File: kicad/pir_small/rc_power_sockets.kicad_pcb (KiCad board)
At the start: 2 copper layers, 25.4 x 25.4 mm, 26 parts, among them IC1 ATTINY85, J1 GND, J2 433MHZ, P1 ICSP, P2 ALT_PWR, Q1 NMOS, Q2 PMOS, U1 MCP1755ST-3302E/DB

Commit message: Changed layout
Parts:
- removed ON   OFF: SWITCH_INV, Buttons_Switches_ThroughHole:SW_Micro_SPST
- removed RV1: POT, Pin_Headers:Pin_Header_Straight_1x03
- added P3: CONN_01X01, theapi_footprints:SMD_PAD, F.Cu at (149.2, 70.4)
- added P4: CONN_01X01, theapi_footprints:SMD_PAD, F.Cu at (149.2, 67.9)
- added SW1: SWITCH_INV, Buttons_Switches_ThroughHole:SW_Micro_SPST, F.Cu at (164.4, 87.0)
- D1, D2, D3: footprint theapi_footprints:SOD-123-Schottky -> theapi_footprints:SOD-123-handsolder
- IC1: footprint theapi_footprints:SOIC-8-N-hand-sold -> theapi_footprints:SOIC-8-N-handsolder
- J1: value GND -> PIR; moved to B.Cu
- P2: footprint Pin_Headers:Pin_Header_Straight_1x02 -> Socket_Strips:Socket_Strip_Straight_1x02
- R5: value 820R -> 820
- moved D4 61.6 mm to (149.2, 82.7), turned to 270 degrees
- moved R5 58.7 mm to (151.6, 82.6), turned to 270 degrees
- moved Q2 54.3 mm to (154.0, 80.1), turned to 90 degrees
- moved D1 51.9 mm to (157.3, 81.2), turned to 0 degrees
- moved D2 51.7 mm to (157.3, 79.1), turned to 0 degrees
- moved C2 48.0 mm to (156.8, 77.6), turned to 180 degrees
- moved R2 47.5 mm to (161.2, 82.0), turned to 180 degrees
- moved U1 46.9 mm to (162.4, 74.8)
- moved Q1 44.7 mm to (154.0, 83.9)
- moved R3 44.5 mm to (149.7, 82.9)
- moved J1 44.0 mm to (170.8, 73.6)
- moved MOUNT6 43.6 mm to (170.8, 65.4)
- moved MOUNT2 43.6 mm to (170.8, 87.0)
- moved J2 43.4 mm to (149.2, 78.7)
- moved IC1 43.4 mm to (157.0, 75.0)
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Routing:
- net /NBASE_ON: track 25.7 -> 8.84 mm
- net /ADC3: track 22.7 -> 7.33 mm
- net /PBASE: track 22.8 -> 9.69 mm
- net /RESET: track 12.1 -> 20.9 mm, vias 1 -> 2
- net /NBASE: track 5.39 -> 14.0 mm
- net /SWITCH_POWER: track 49.2 -> 42.8 mm, vias 3 -> 0
- net /VCC: track 5.59 -> 2.79 mm
- net /MISO: track 21.3 -> 23.8 mm
- net GND: track 121.1 -> 123.2 mm, vias 4 -> 3
- net /3.3v: track 32.3 -> 30.5 mm
- net /SCK: track 33.4 -> 31.7 mm, vias 0 -> 1
- net /MOSI: track 34.8 -> 33.4 mm
- net /POWER: track 22.8 -> 22.0 mm
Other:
- board size 25.4 x 25.4 mm -> 25 x 25 mm

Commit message: Silkscreen
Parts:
- P3, P4: footprint theapi_footprints:SMD_PAD -> Pin_Headers:Pin_Header_Straight_1x01
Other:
- board text added: "+"
- board text added: "-"
- board text added: "1"
- board text added: "A0"
- board text added: "D"
- board text added: "ON OFF"
- board text added: "PIR"
- board text added: "RC Power Sockets Small v1.0"
- board text removed: "GND"
- board text removed: "RC Power Sockets v2.0"
- board text removed: "SCK"
- board text removed: "VCC"

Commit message: Power pins
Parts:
- P2: footprint Socket_Strips:Socket_Strip_Straight_1x02 -> Pin_Headers:Pin_Header_Straight_1x02
- turned P2 to 90 degrees
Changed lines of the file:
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@@
     (links 49)
     (no_connects 0)
-    (area 147.382999 63.582999 172.533001 88.733001)
+    (area 144.000667 61.624 175.915334 93.082)
     (thickness 1.6)
-    (drawings 35)
+    (drawings 33)
     (tracks 197)
     (zones 0)
@@
   (page A4)
   (layers
-    (0 F.Cu signal hide)
-    (31 B.Cu signal hide)
+    (0 F.Cu signal)
+    (31 B.Cu signal)
     (32 B.Adhes user)
     (33 F.Adhes user)
@@
     (35 F.Paste user)
     (36 B.SilkS user)
-    (37 F.SilkS user hide)
+    (37 F.SilkS user)
     (38 B.Mask user)
     (39 F.Mask user)
@@
     )
   )
-  (module Socket_Strips:Socket_Strip_Straight_1x02 (layer F.Cu)
-    (at 156.529 86.953)
-    (descr "Through hole socket strip")
-    (tags "socket strip")
-    (fp_text reference P2 (at 0 -5.1) (layer F.SilkS) hide
-      (effects (font (size 1 1) (thickness 0.15)))
-    )
-    (fp_text value ALT_PWR (at 0 -3.1) (layer F.Fab) hide
-      (effects (font (size 1 1) (thickness 0.15)))
-    )
-    (fp_line (start -1.55 1.55) (end 0 1.55) (layer F.SilkS) (width 0.15))
-    (fp_line (start 3.81 1.27) (end 1.27 1.27) (layer F.SilkS) (width 0.15))
-    (fp_line (start -1.75 -1.75) (end -1.75 1.75) (layer F.CrtYd) (width 0.05))
-    (fp_line (start 4.3 -1.75) (end 4.3 1.75) (layer F.CrtYd) (width 0.05))
-    (fp_line (start -1.75 -1.75) (end 4.3 -1.75) (layer F.CrtYd) (width 0.05))
-    (fp_line (start -1.75 1.75) (end 4.3 1.75) (layer F.CrtYd) (width 0.05))
-    (fp_line (start 1.27 1.27) (end 1.27 -1.27) (layer F.SilkS) (width 0.15))
-    (fp_line (start 0 -1.55) (end -1.55 -1.55) (layer F.SilkS) (width 0.15))
-    (fp_line (start -1.55 -1.55) (end -1.55 1.55) (layer F.SilkS) (width 0.15))
-    (fp_line (start 1.27 -1.27) (end 3.81 -1.27) (layer F.SilkS) (width 0.15))
-    (fp_line (start 3.81 -1.27) (end 3.81 1.27) (layer F.SilkS) (width 0.15))
-    (pad 1 thru_hole rect (at 0 0) (size 2.032 2.032) (drill 1.016) (layers *.Cu *.Mask F.SilkS)
-      (net 1 GND))
-    (pad 2 thru_hole oval (at 2.54 0) (size 2.032 2.032) (drill 1.016) (layers *.Cu *.Mask F.SilkS)
-      (net 16 /VCC))
-    (model Socket_Strips.3dshapes/Socket_Strip_Straight_1x02.wrl
-      (at (xyz 0.05 0 0))
-      (scale (xyz 1 1 1))
-      (rotate (xyz 0 0 180))
-    )
-  )
   (module Pin_Headers:Pin_Header_Straight_1x01 (layer F.Cu)
     (at 149.163 70.443)
@@
     )
   )
+  (module Pin_Headers:Pin_Header_Straight_1x02 (layer F.Cu)
+    (at 156.529 86.953 90)
+    (descr "Through hole pin header")
+    (tags "pin header")
+    (fp_text reference P2 (at 0 -5.1 90) (layer F.SilkS) hide
+      (effects (font (size 1 1) (thickness 0.15)))
+    )
+    (fp_text value ALT_PWR (at 0 -3.1 90) (layer F.Fab) hide
+      (effects (font (size 1 1) (thickness 0.15)))
+    )
+    (fp_line (start 1.27 1.27) (end 1.27 3.81) (layer F.SilkS) (width 0.15))
+    (fp_line (start 1.55 -1.55) (end 1.55 0) (layer F.SilkS) (width 0.15))
+    (fp_line (start -1.75 -1.75) (end -1.75 4.3) (layer F.CrtYd) (width 0.05))
+    (fp_line (start 1.75 -1.75) (end 1.75 4.3) (layer F.CrtYd) (width 0.05))
+    (fp_line (start -1.75 -1.75) (end 1.75 -1.75) (layer F.CrtYd) (width 0.05))
+    (fp_line (start -1.75 4.3) (end 1.75 4.3) (layer F.CrtYd) (width 0.05))
+    (fp_line (start 1.27 1.27) (end -1.27 1.27) (layer F.SilkS) (width 0.15))
+    (fp_line (start -1.55 0) (end -1.55 -1.55) (layer F.SilkS) (width 0.15))
+    (fp_line (start -1.55 -1.55) (end 1.55 -1.55) (layer F.SilkS) (width 0.15))
+    (fp_line (start -1.27 1.27) (end -1.27 3.81) (layer F.SilkS) (width 0.15))
+    (fp_line (start -1.27 3.81) (end 1.27 3.81) (layer F.SilkS) (width 0.15))
+    (pad 1 thru_hole rect (at 0 0 90) (size 2.032 2.032) (drill 1.016) (layers *.Cu *.Mask F.SilkS)
+      (net 1 GND))
+    (pad 2 thru_hole oval (at 0 2.54 90) (size 2.032 2.032) (drill 1.016) (layers *.Cu *.Mask F.SilkS)
+      (net 16 /VCC))
+    (model Pin_Headers.3dshapes/Pin_Header_Straight_1x02.wrl
+      (at (xyz 0 -0.05 0))
+      (scale (xyz 1 1 1))
+      (rotate (xyz 0 0 90))
+    )
+  )
   (gr_text A0 (at 151.449 70.316) (layer B.SilkS)
     (effects (font (size 1.016 1.016) (thickness 0.1524)) (justify mirror))
@@
     (effects (font (size 1.016 1.016) (thickness 0.1524)))
   )
-  (gr_line (start 142.458 76.158) (end 174.958 76.158) (angle 90) (layer Cmts.User) (width 0.2))
-  (gr_line (start 159.958 56.158) (end 159.958 91.158) (angle 90) (layer Cmts.User) (width 0.2))
   (gr_line (start 147.458 88.658) (end 147.458 63.658) (angle 90) (layer Edge.Cuts) (width 0.15))
   (gr_line (start 172.458 88.658) (end 147.458 88.658) (angle 90) (layer Edge.Cuts) (width 0.15))

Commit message: Logo
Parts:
- added REF**: TheApiLogo, theapi_footprints:TheApiLogoSmall, F.Cu at (165.7, 73.9)
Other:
- board text added: "petermclarke @gmail.com"

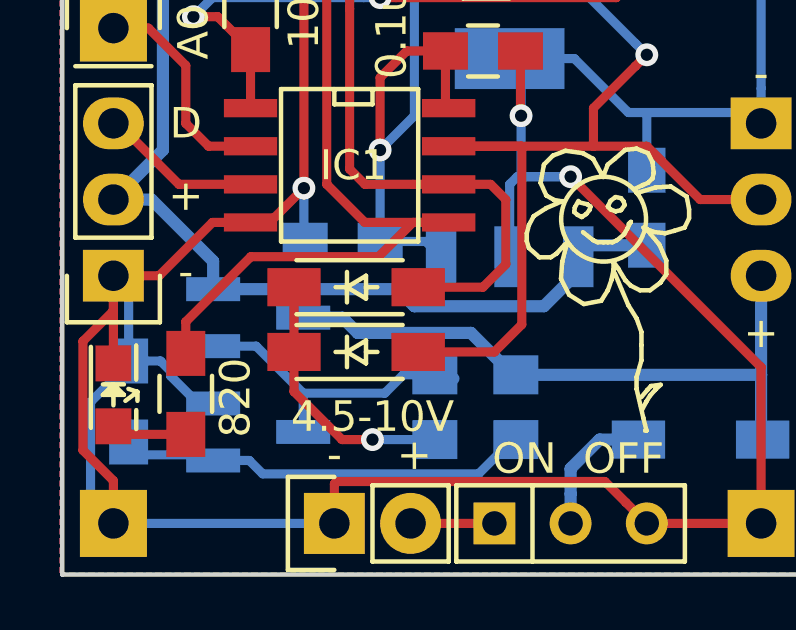
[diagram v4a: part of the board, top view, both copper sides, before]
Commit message: Corrected pchannel mosfet
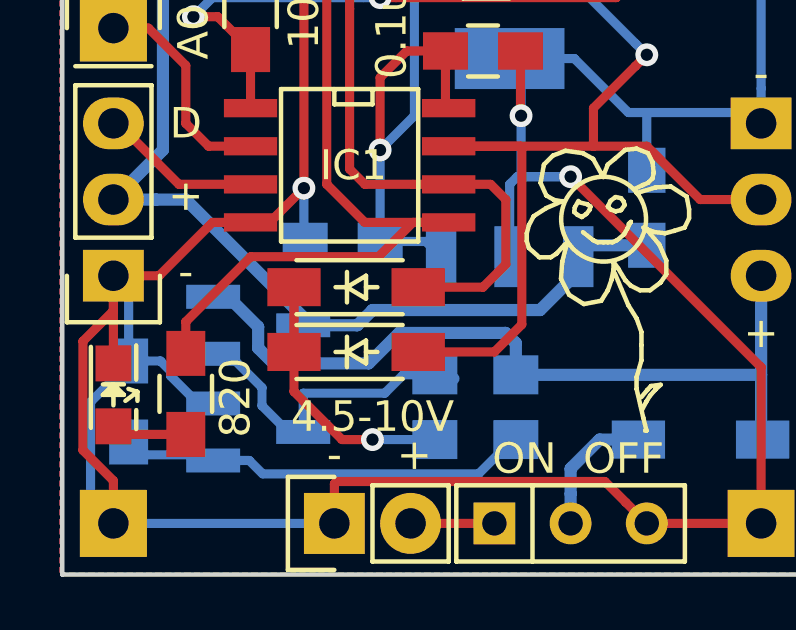
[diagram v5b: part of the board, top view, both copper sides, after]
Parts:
- moved Q2 0.25 mm to (154.0, 80.3)
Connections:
- Q2 pad 2: /SWITCH_POWER -> /POWER
- Q2 pad 3: /POWER -> /SWITCH_POWER
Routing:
- net /POWER: track 22.0 -> 26.8 mm
- net /PBASE: track 9.69 -> 10.5 mm
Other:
- board text added: "RC Power Sockets Small v1.1"
- board text removed: "RC Power Sockets Small v1.0"
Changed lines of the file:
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@@
-(kicad_pcb (version 4) (host pcbnew 4.0.1-stable)
+(kicad_pcb (version 4) (host pcbnew 4.0.2-stable)
   (general
     (links 49)
     (no_connects 0)
-    (area 147.382999 63.582999 172.533001 88.733001)
+    (area 144.000667 61.624 175.915334 93.082)
     (thickness 1.6)
     (drawings 34)
-    (tracks 197)
+    (tracks 205)
     (zones 0)
     (modules 28)
@@
   )
   (module TO_SOT_Packages_SMD:SOT-23_Handsoldering (layer B.Cu)
-    (at 153.989 80.095 90)
+    (at 153.989 80.349 90)
     (descr "SOT-23, Handsoldering")
     (tags SOT-23)
@@
       (net 11 /PBASE))
     (pad 2 smd rect (at 0.95 -1.50114 90) (size 0.8001 1.80086) (layers B.Cu B.Paste B.Mask)
+      (net 13 /POWER))
+    (pad 3 smd rect (at 0 1.50114 90) (size 0.8001 1.80086) (layers B.Cu B.Paste B.Mask)
       (net 8 /SWITCH_POWER))
-    (pad 3 smd rect (at 0 1.50114 90) (size 0.8001 1.80086) (layers B.Cu B.Paste B.Mask)
-      (net 13 /POWER))
     (model TO_SOT_Packages_SMD.3dshapes/SOT-23_Handsoldering.wrl
       (at (xyz 0 0 0))
@@
     (effects (font (size 1.016 1.016) (thickness 0.1524)))
   )
-  (gr_text "RC\nPower\nSockets\nSmall\nv1.0" (at 156.402 68.792) (layer B.SilkS)
+  (gr_text "RC\nPower\nSockets\nSmall\nv1.1" (at 156.402 68.792) (layer B.SilkS)
     (effects (font (size 1.016 1.016) (thickness 0.1524) italic) (justify mirror))
   )
@@
   (segment (start 151.576 71.6876) (end 151.576 73.618) (width 0.3048) (layer F.Cu) (net 7))
   (segment (start 151.576 73.618) (end 152.338 74.38) (width 0.3048) (layer F.Cu) (net 7))
-  (segment (start 152.48786 79.145) (end 158.627 79.145) (width 0.4064) (layer B.Cu) (net 8))
-  (segment (start 159.196 79.714) (end 163.514 79.714) (width 0.4064) (layer B.Cu) (net 8))
-  (segment (start 158.627 79.145) (end 159.196 79.714) (width 0.4064) (layer B.Cu) (net 8))
-  (segment (start 163.514 79.714) (end 164.657 78.571) (width 0.4064) (layer B.Cu) (net 8))
+  (segment (start 155.49014 80.349) (end 155.49014 80.07214) (width 0.4064) (layer B.Cu) (net 8))
+  (segment (start 155.49014 80.07214) (end 151.576 76.158) (width 0.4064) (layer B.Cu) (net 8))
+  (segment (start 151.576 76.158) (end 150.5854 76.158) (width 0.4064) (layer B.Cu) (net 8))
+  (segment (start 150.5854 76.158) (end 149.163 76.158) (width 0.4064) (layer B.Cu) (net 8))
+  (segment (start 155.49014 80.349) (end 157.291 80.349) (width 0.4064) (layer B.Cu) (net 8))
+  (segment (start 163.387 79.841) (end 164.657 78.571) (width 0.4064) (layer B.Cu) (net 8))
+  (segment (start 157.291 80.349) (end 157.799 79.841) (width 0.4064) (layer B.Cu) (net 8))
   (segment (start 164.657 78.571) (end 164.657 78.063) (width 0.4064) (layer B.Cu) (net 8))
-  (segment (start 152.48786 79.145) (end 152.48786 78.21286) (width 0.4064) (layer B.Cu) (net 8))
-  (segment (start 152.48786 78.21286) (end 150.433 76.158) (width 0.4064) (layer B.Cu) (net 8))
-  (segment (start 150.433 76.158) (end 149.163 76.158) (width 0.4064) (layer B.Cu) (net 8))
+  (segment (start 157.799 79.841) (end 163.387 79.841) (width 0.4064) (layer B.Cu) (net 8))
   (segment (start 166.943 77.682) (end 165.038 77.682) (width 0.4064) (layer B.Cu) (net 8))
   (segment (start 165.038 77.682) (end 164.657 78.063) (width 0.4064) (layer B.Cu) (net 8))
@@
   (segment (start 150.099 84.667) (end 152.29986 84.667) (width 0.3048) (layer B.Cu) (net 10))
   (segment (start 152.385 84.95786) (end 152.48786 84.855) (width 0.3048) (layer B.Cu) (net 10))
+  (segment (start 152.48786 81.299) (end 152.98824 81.299) (width 0.3048) (layer B.Cu) (net 11))
+  (segment (start 154.116 82.42676) (end 154.116 83.03124) (width 0.3048) (layer B.Cu) (net 11))
+  (segment (start 152.98824 81.299) (end 154.116 82.42676) (width 0.3048) (layer B.Cu) (net 11))
+  (segment (start 154.116 83.03124) (end 154.98976 83.905) (width 0.3048) (layer B.Cu) (net 11))
+  (segment (start 154.98976 83.905) (end 155.49014 83.905) (width 0.3048) (layer B.Cu) (net 11))
   (segment (start 159.878 82) (end 158.8232 82) (width 0.3048) (layer B.Cu) (net 11))
   (segment (start 158.8232 82) (end 158.21106 82.61214) (width 0.3048) (layer B.Cu) (net 11))
   (segment (start 158.21106 82.61214) (end 155.49014 82.61214) (width 0.3048) (layer B.Cu) (net 11))
-  (segment (start 152.48786 81.045) (end 153.923 81.045) (width 0.3048) (layer B.Cu) (net 11))
-  (segment (start 153.923 81.045) (end 155.49014 82.61214) (width 0.3048) (layer B.Cu) (net 11))
   (segment (start 155.49014 82.61214) (end 155.49014 83.20015) (width 0.3048) (layer B.Cu) (net 11))
   (segment (start 155.49014 83.20015) (end 155.49014 83.905) (width 0.3048) (layer B.Cu) (net 11))
@@
   (via (at 157.799 84.158994) (size 0.762) (drill 0.4064) (layers F.Cu B.Cu) (net 12))
   (segment (start 155.1828 79.079) (end 155.1828 81.238) (width 0.3048) (layer F.Cu) (net 12))
+  (segment (start 162.578 82) (end 162.578 80.9436) (width 0.4064) (layer B.Cu) (net 13))
+  (segment (start 162.578 80.9436) (end 162.2374 80.603) (width 0.4064) (layer B.Cu) (net 13))
+  (segment (start 162.2374 80.603) (end 158.688 80.603) (width 0.4064) (layer B.Cu) (net 13))
+  (segment (start 158.688 80.603) (end 157.672 81.619) (width 0.4064) (layer B.Cu) (net 13))
+  (segment (start 157.672 81.619) (end 154.497 81.619) (width 0.4064) (layer B.Cu) (net 13))
+  (segment (start 154.497 81.619) (end 153.989 81.111) (width 0.4064) (layer B.Cu) (net 13))
+  (segment (start 153.989 80.39976) (end 152.98824 79.399) (width 0.4064) (layer B.Cu) (net 13))
+  (segment (start 153.989 81.111) (end 153.989 80.39976) (width 0.4064) (layer B.Cu) (net 13))
+  (segment (start 152.98824 79.399) (end 152.48786 79.399) (width 0.4064) (layer B.Cu) (net 13))
   (segment (start 170.753 78.698) (end 170.753 82) (width 0.4064) (layer B.Cu) (net 13))
   (segment (start 170.753 82) (end 170.753 84.1082) (width 0.4064) (layer B.Cu) (net 13))
   (segment (start 162.578 82) (end 170.753 82) (width 0.4064) (layer B.Cu) (net 13))
-  (segment (start 155.49014 80.095) (end 156.79697 80.095) (width 0.4064) (layer B.Cu) (net 13))
-  (segment (start 156.79697 80.095) (end 157.30497 80.603) (width 0.4064) (layer B.Cu) (net 13))
-  (segment (start 157.30497 80.603) (end 161.081 80.603) (width 0.4064) (layer B.Cu) (net 13))
-  (segment (start 161.081 80.603) (end 162.478 82) (width 0.4064) (layer B.Cu) (net 13))
   (segment (start 162.478 82) (end 162.578 82) (width 0.4064) (layer B.Cu) (net 13))
   (segment (start 170.753 84.1082) (end 170.8038 84.159) (width 0.4064) (layer B.Cu) (net 13))
-  (segment (start 155.49014 80.095) (end 155.99052 80.095) (width 0.4064) (layer B.Cu) (net 13))
   (segment (start 151.576 83.985) (end 149.43096 83.985) (width 0.3048) (layer F.Cu) (net 14))
   (segment (start 149.43096 83.985) (end 149.163 83.71704) (width 0.3048) (layer F.Cu) (net 14))
